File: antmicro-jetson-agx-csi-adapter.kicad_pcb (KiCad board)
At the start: 4 copper layers, 73.6 x 41 mm, 104 parts, among them IC1 MAX1708EEE+, J1 QTH-060-03-L-D-A, J2 WE_68715014522_ONE-SIDE, J3 WE_68715014022, J4 BM04B-SRSS-TB-LF-SN, J5 SM06B-SRSS-TB(LF)(SN), J6 SM09B-SRSS-TB(LF)(SN), J7 61300611121, Q1 BSS138AKA, U1 PCA9547BS,118, U2 NTS0102DP

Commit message: Routed all the signals
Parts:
- moved TP2 124.4 mm to (167.4, 107.6)
- moved TP3 121.9 mm to (167.4, 106.5)
- moved TP1 120.4 mm to (170.5, 105.6)
- moved TP7 119.9 mm to (170.5, 106.8)
- moved TP6 116.0 mm to (168.6, 103.9)
- moved TP4 110.2 mm to (167.4, 105.4)
- moved TP5 108.3 mm to (167.3, 103.9)
- moved TP9 104.8 mm to (160.4, 93.9)
- moved TP11 103.9 mm to (155.5, 72.2)
- moved TP10 99.5 mm to (149.0, 97.9)
- moved TP8 84.3 mm to (131.5, 104.2)
- moved TP23 81.0 mm to (154.2, 94.0)
- moved C6 17.1 mm to (150.1, 99.2), turned to 90 degrees
- moved TP21 11.8 mm to (152.8, 101.7), turned to 180 degrees
- moved U2 11.6 mm to (153.9, 99.1), turned to -90 degrees
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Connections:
- J1 pad G1: (no net) -> GND
- J1 pad G2: (no net) -> GND
- J1 pad G3: (no net) -> GND
- J1 pad G4: (no net) -> GND
- J1 pad G5: (no net) -> GND
- J1 pad G6: (no net) -> GND
- J1 pad G7: (no net) -> GND
- J1 pad G8: (no net) -> GND
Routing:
- net GND: track 7.58 -> 147.9 mm, vias 6 -> 79
- net /Auxiliary/DEPTH_CAM_SYNC_3V3: track 11.0 -> 67.6 mm, vias 0 -> 2
- net +3V3: track 3.10 -> 49.7 mm, vias 0 -> 21
- net DVDD_CAM_LV: track 0.00 -> 34.1 mm, vias 0 -> 1
- net AVDD_CAM_2V8: track 0.00 -> 24.9 mm, vias 0 -> 1
- net +1V8: track 6.16 -> 26.1 mm, vias 0 -> 1
- net /Interface/3V3_FFC_B: track 5.25 -> 17.1 mm, vias 0 -> 2
- net /Interface/I2C_GP2_CLK: track 0.00 -> 10.2 mm, vias 0 -> 1
- net I2C_GP3_CLK: track 17.4 -> 7.31 mm
- net /Interface/I2C_GP2_DAT: track 0.00 -> 9.44 mm, vias 0 -> 1
- net I2C_GP3_DAT: track 13.2 -> 4.17 mm
- net DVDD_CAM_IO: track 0.00 -> 8.92 mm, vias 0 -> 1
- net /Interface/CAM0_PWDN: track 0.00 -> 8.44 mm, vias 0 -> 1
- net CAM0_SDA: track 20.0 -> 28.4 mm
- net +5V: track 0.00 -> 6.97 mm, vias 0 -> 10
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- added copper zone on F.Cu, net +3V3
- added copper zone on In2.Cu, net +3V3
- added copper zone on B.Cu, net +5V
- added copper zone on F.Cu, net +5V
- added copper zone on In2.Cu, net +5V
- added copper zone on F.Cu, net /Interface/5V_FFC_B
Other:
- board text removed: "TODO: FIX FOOTPRINT"

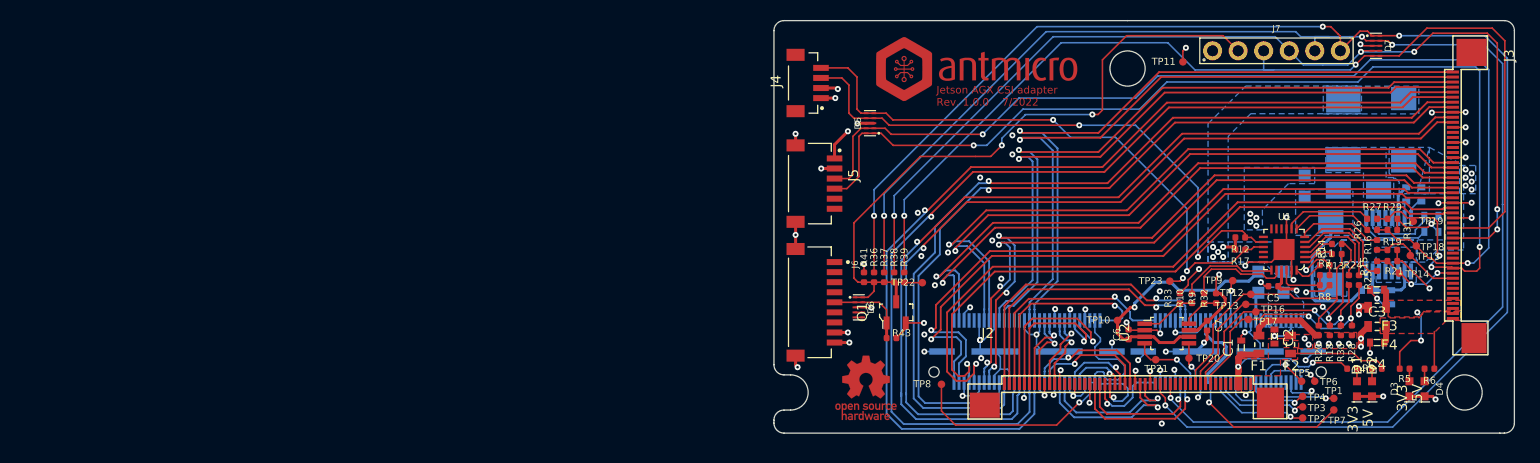
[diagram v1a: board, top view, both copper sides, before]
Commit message: Removed AUX connector and changed SYNC connector package
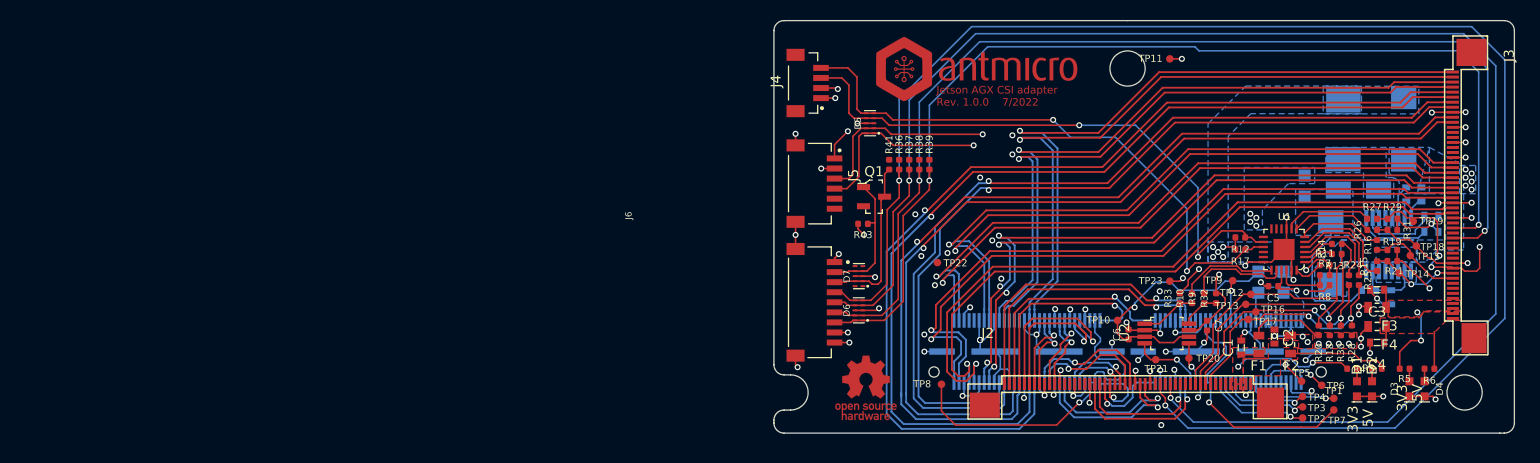
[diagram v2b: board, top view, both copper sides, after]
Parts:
- removed J7: 61300611121, antmicro-footprints:61300611121
- moved D7 56.3 mm to (123.3, 93.4), turned to 90 degrees
- moved Q1 11.7 mm to (124.8, 85.5), turned to 0 degrees
- moved R43 11.7 mm to (123.7, 88.2), turned to 0 degrees
- moved R37 11.5 mm to (128.3, 82.3), turned to 90 degrees
- moved R38 11.5 mm to (129.3, 82.3), turned to 90 degrees
- moved R39 11.5 mm to (130.3, 82.3), turned to 90 degrees
- moved R36 11.5 mm to (127.3, 82.3), turned to 90 degrees
- moved R41 11.5 mm to (126.3, 82.3)
- moved TP22 2.50 mm to (131.1, 92.1)
- moved TP11 1.33 mm to (154.2, 71.9)
- moved TP6 0.81 mm to (169.3, 104.3)
- moved D6 0.30 mm to (123.3, 96.8), turned to 90 degrees
- moved C8 0.10 mm to (177.4, 78.8)
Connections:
- D6 pad 1: /Auxiliary/DEPTH_CAM_SYNC_3V3 -> VSYNC_CAM3_3V3
- D6 pad 10: /Auxiliary/DEPTH_CAM_SYNC_3V3 -> VSYNC_CAM3_3V3
- D6 pad 2: /Auxiliary/DEPTH_CAM_SYNC -> VSYNC_CAM2_3V3
- D6 pad 4: Net-(D6-Pad4) -> VSYNC_CAM1_3V3
- D6 pad 5: Net-(D6-Pad5) -> VSYNC_CAM0_3V3
- D6 pad 6: Net-(D6-Pad5) -> VSYNC_CAM0_3V3
- D6 pad 7: Net-(D6-Pad4) -> VSYNC_CAM1_3V3
- D6 pad 9: /Auxiliary/DEPTH_CAM_SYNC -> VSYNC_CAM2_3V3
- D7 pad 1: VSYNC_CAM0_3V3 -> unconnected-(D7-Pad1)
- D7 pad 10: VSYNC_CAM0_3V3 -> unconnected-(D7-Pad1)
- D7 pad 2: VSYNC_CAM1_3V3 -> /Auxiliary/CAM_SYNC_3V3
- D7 pad 4: VSYNC_CAM2_3V3 -> /Auxiliary/CAM_SYNC
- D7 pad 5: VSYNC_CAM3_3V3 -> unconnected-(D7-Pad5)
- D7 pad 6: VSYNC_CAM3_3V3 -> unconnected-(D7-Pad5)
- D7 pad 7: VSYNC_CAM2_3V3 -> /Auxiliary/CAM_SYNC
- D7 pad 9: VSYNC_CAM1_3V3 -> /Auxiliary/CAM_SYNC_3V3
- J1 pad G1: GND -> (no net)
- J1 pad G2: GND -> (no net)
- J1 pad G3: GND -> (no net)
- J1 pad G4: GND -> (no net)
- J1 pad G5: GND -> (no net)
- J1 pad G6: GND -> (no net)
- J1 pad G7: GND -> (no net)
- J1 pad G8: GND -> (no net)
- J6 pad 1: /Auxiliary/GPIO3 -> GND
- J6 pad 2: /Auxiliary/GPIO4 -> /Auxiliary/CAM_SYNC
- J6 pad 3: /Auxiliary/GPIO5 -> /Auxiliary/CAM_SYNC_3V3
- J6 pad 4: /Auxiliary/GPIO6 -> VSYNC_CAM0_3V3
- J6 pad 5: /Auxiliary/DEPTH_CAM_SYNC -> VSYNC_CAM1_3V3
- J6 pad 6: /Auxiliary/LASER_PWM0 -> VSYNC_CAM2_3V3
- J6 pad 7: /Auxiliary/LASER_PWM1 -> VSYNC_CAM3_3V3
- Q1 pad 1: /Auxiliary/DEPTH_CAM_SYNC -> /Auxiliary/CAM_SYNC
- Q1 pad 3: /Auxiliary/DEPTH_CAM_SYNC_3V3 -> /Auxiliary/CAM_SYNC_3V3
- R36 pad 2: /Auxiliary/DEPTH_CAM_SYNC_3V3 -> /Auxiliary/CAM_SYNC_3V3
- R37 pad 2: /Auxiliary/DEPTH_CAM_SYNC_3V3 -> /Auxiliary/CAM_SYNC_3V3
- R38 pad 2: /Auxiliary/DEPTH_CAM_SYNC_3V3 -> /Auxiliary/CAM_SYNC_3V3
- R39 pad 2: /Auxiliary/DEPTH_CAM_SYNC_3V3 -> /Auxiliary/CAM_SYNC_3V3
- R41 pad 1: /Auxiliary/DEPTH_CAM_SYNC_3V3 -> /Auxiliary/CAM_SYNC_3V3
- R43 pad 2: /Auxiliary/DEPTH_CAM_SYNC -> /Auxiliary/CAM_SYNC
- TP22 pad 1: /Auxiliary/DEPTH_CAM_SYNC_3V3 -> /Auxiliary/CAM_SYNC_3V3
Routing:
- net CAM3_SDA: track 103.9 -> 29.7 mm
- net CAM3_SCL: track 108.9 -> 37.8 mm
- net /Auxiliary/DEPTH_CAM_SYNC_3V3: track 67.6 -> 0.00 mm, vias 2 -> 0
- net /Auxiliary/CAM_SYNC_3V3: track 0.00 -> 16.5 mm
- net /Auxiliary/CAM_SYNC: track 0.00 -> 13.3 mm
- net VSYNC_CAM0_3V3: track 148.9 -> 158.0 mm, vias 4 -> 2
- net VSYNC_CAM1_3V3: track 144.5 -> 153.2 mm, vias 4 -> 2
- net /Auxiliary/DEPTH_CAM_SYNC: track 8.29 -> 0.00 mm
- net VSYNC_CAM2_3V3: track 102.2 -> 108.5 mm, vias 5 -> 2
- net VSYNC_CAM3_3V3: track 102.4 -> 105.1 mm
- net /Interface/3V3_FFC_B: track 17.1 -> 14.6 mm
- net GND: track 147.9 -> 146.7 mm
- net +3V3: track 49.7 -> 48.6 mm, vias 21 -> 20
- net Net-(D6-Pad5): track 0.77 -> 0.00 mm
- net Net-(D6-Pad4): track 0.77 -> 0.00 mm
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- added copper zone on F.Cu, net /Interface/3V3_FFC_B

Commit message: Rerouted tracks after connector change
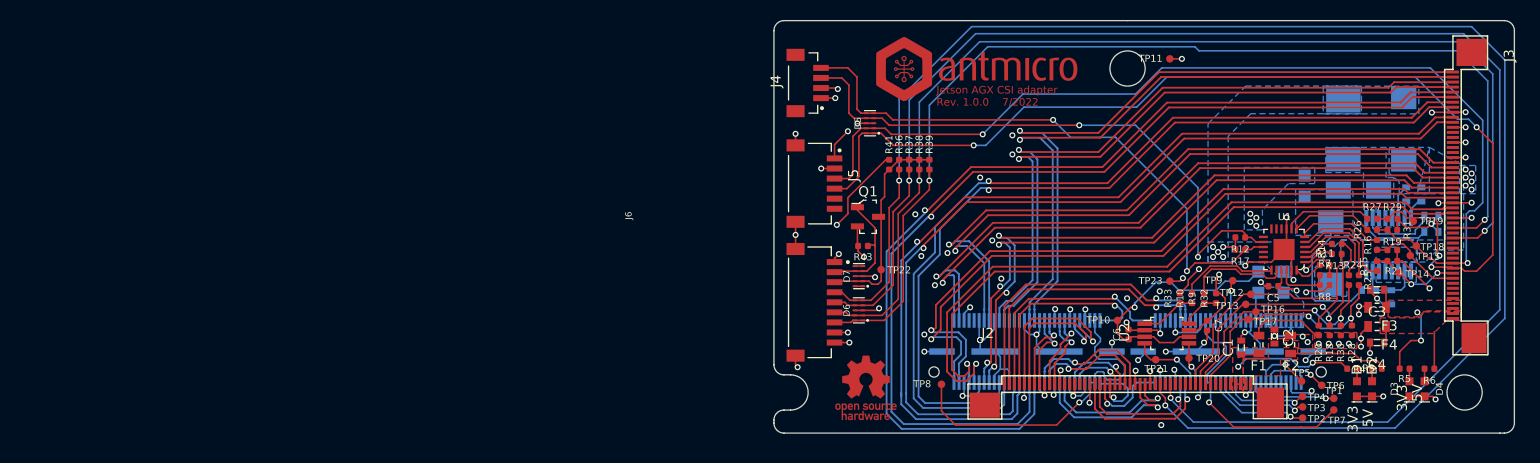
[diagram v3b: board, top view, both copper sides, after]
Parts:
- moved TP22 5.64 mm to (125.5, 92.8)
- moved R43 2.20 mm to (123.7, 90.4)
- moved Q1 2.09 mm to (124.2, 87.5)
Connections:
- J1 pad G1: (no net) -> GND
- J1 pad G2: (no net) -> GND
- J1 pad G3: (no net) -> GND
- J1 pad G4: (no net) -> GND
- J1 pad G5: (no net) -> GND
- J1 pad G6: (no net) -> GND
- J1 pad G7: (no net) -> GND
- J1 pad G8: (no net) -> GND
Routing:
- net CAM3_SDA: track 29.7 -> 99.5 mm
- net CAM3_SCL: track 37.8 -> 105.7 mm
- net +3V3: track 48.6 -> 57.4 mm, vias 20 -> 21
- net /Auxiliary/CAM_SYNC_3V3: track 16.5 -> 20.7 mm
- net GND: track 146.7 -> 148.7 mm
- net /Auxiliary/CAM_SYNC: track 13.3 -> 11.5 mm
- net VSYNC_CAM3_3V3: track 105.1 -> 105.9 mm
- net unconnected-(D7-Pad5): track 0.00 -> 0.78 mm
- net unconnected-(D7-Pad1): track 0.00 -> 0.78 mm

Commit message: Length matched CSI signals
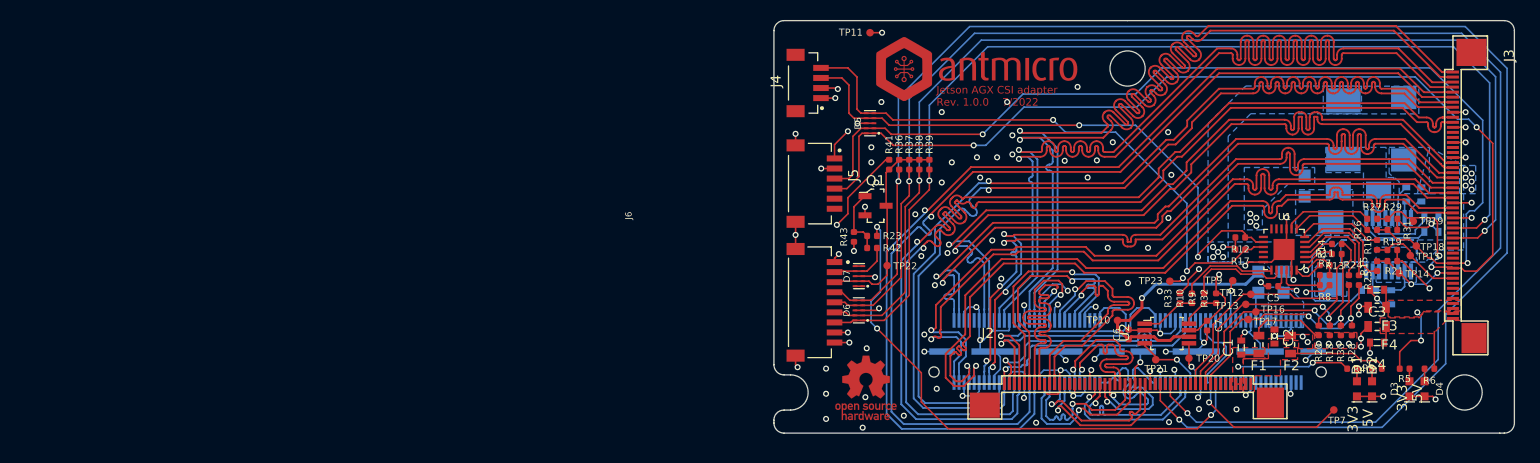
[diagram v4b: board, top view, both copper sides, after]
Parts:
- removed TP1, TP2, TP3, TP4, TP5, TP6, TP8: TP_SMD_0_75MM, antmicro-footprints:Testpoint_smd_0_75mm
- added R23: R_0R_0402, antmicro-footprints:0402-res, F.Cu at (124.6, 89.4)
- added R42: R_0R_0402, antmicro-footprints:0402-res, F.Cu at (124.6, 90.6)
- moved TP11 29.9 mm to (124.4, 69.3)
- moved Q1 1.33 mm to (125.0, 86.4)
- moved R43 1.27 mm to (122.8, 89.5), turned to 90 degrees
- moved TP22 0.72 mm to (126.1, 92.4)
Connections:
- D7 pad 4: /Auxiliary/CAM_SYNC -> /Auxiliary/EXT_CAM_SYNC
- D7 pad 7: /Auxiliary/CAM_SYNC -> /Auxiliary/EXT_CAM_SYNC
- J1 pad 101: DVDD_CAM_IO -> unconnected-(J1-Pad101)
- J1 pad 103: /Interface/SNN_FLASH_MASK -> unconnected-(J1-Pad103)
- J1 pad 104: /Interface/SNN_TORCH_EN -> unconnected-(J1-Pad104)
- J1 pad 105: /Interface/I2C_GP4_CLK -> unconnected-(J1-Pad105)
- J1 pad 106: /Interface/SNN_FLASH_STROBE -> unconnected-(J1-Pad106)
- J1 pad 107: /Interface/I2C_GP4_DAT -> unconnected-(J1-Pad107)
- J1 pad 109: /Interface/VDD_IR -> unconnected-(J1-Pad109)
- J1 pad 111: /Interface/SNN_SPI_SCK -> unconnected-(J1-Pad111)
- J1 pad 112: /Interface/SNN_SPI_DIN -> unconnected-(J1-Pad112)
- J1 pad 113: /Interface/SNN_SPI_CS0 -> unconnected-(J1-Pad113)
- J1 pad 114: /Interface/SNN_SPI_DOUT -> unconnected-(J1-Pad114)
- J1 pad 117: /Interface/CAM_INTR -> unconnected-(J1-Pad117)
- J1 pad 119: /Interface/GPIO25_VDD_SYS_EN -> unconnected-(J1-Pad119)
- J1 pad 55: DVDD_CAM_LV -> unconnected-(J1-Pad55)
- J1 pad 56: DVDD_CAM_LV -> unconnected-(J1-Pad56)
- J1 pad 57: DVDD_CAM_LV -> unconnected-(J1-Pad57)
- J1 pad 58: DVDD_CAM_LV -> unconnected-(J1-Pad58)
- J1 pad 76: /Interface/SNN_CAM_76 -> unconnected-(J1-Pad76)
- J1 pad 78: /Interface/SNN_CAM_HSYNC -> unconnected-(J1-Pad78)
- J1 pad 84: /Interface/VDD_AF -> unconnected-(J1-Pad84)
- J1 pad 85: /Interface/CAM_AF_PWDN -> GPIO10
- J1 pad 86: /Interface/SNN_CAM_VSYNC -> unconnected-(J1-Pad86)
- J1 pad 87: /Interface/I2C_GP2_CLK -> unconnected-(J1-Pad87)
- J1 pad 88: /Interface/CAM1_MCLK03 -> unconnected-(J1-Pad88)
- J1 pad 89: /Interface/I2C_GP2_DAT -> unconnected-(J1-Pad89)
- J1 pad 90: /Interface/CAM1_PWDN -> unconnected-(J1-Pad90)
- J1 pad 91: /Interface/CAM0_MCLK02 -> unconnected-(J1-Pad91)
- J1 pad 93: /Interface/CAM0_PWDN -> unconnected-(J1-Pad93)
- J1 pad 94: /Interface/CAM2_MCLK04 -> unconnected-(J1-Pad94)
- J1 pad 95: /Interface/CAM0_RST_BUFFER -> unconnected-(J1-Pad95)
- J1 pad 96: /Interface/SNN_CAM2_PWDN -> unconnected-(J1-Pad96)
- J1 pad 97: /Interface/SNN_FLASH_EN -> unconnected-(J1-Pad97)
- J1 pad 98: /Interface/SNN_CAM2_RST -> unconnected-(J1-Pad98)
- J6 pad 2: /Auxiliary/CAM_SYNC -> /Auxiliary/EXT_CAM_SYNC
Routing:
- net GPIO10: track 0.00 -> 54.8 mm, vias 0 -> 3
- net /Interface/CSI3_D0_P: track 65.2 -> 99.7 mm
- net DVDD_CAM_LV: track 34.1 -> 0.00 mm, vias 1 -> 0
- net /Interface/CSI3_D0_N: track 66.0 -> 99.7 mm
- net /Interface/CSI3_D1_P: track 67.4 -> 99.9 mm
- net /Interface/CSI3_D1_N: track 68.2 -> 99.9 mm
- net /Interface/CSI6_CLK_P: track 7.92 -> 23.9 mm
- net /Interface/CSI6_D0_N: track 7.84 -> 23.8 mm
- net /Interface/CSI6_CLK_N: track 8.04 -> 23.9 mm
- net /Interface/CSI2_D0_P: track 84.6 -> 100.4 mm
- net /Interface/CSI6_D0_P: track 7.98 -> 23.8 mm
- net /Interface/CSI2_D0_N: track 87.0 -> 100.5 mm
- net /Interface/CSI1_D0_P: track 62.1 -> 73.8 mm
- net /Interface/CSI2_CLK_P: track 88.5 -> 100.2 mm
- net /Interface/CSI4_D1_N: track 5.77 -> 16.0 mm
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
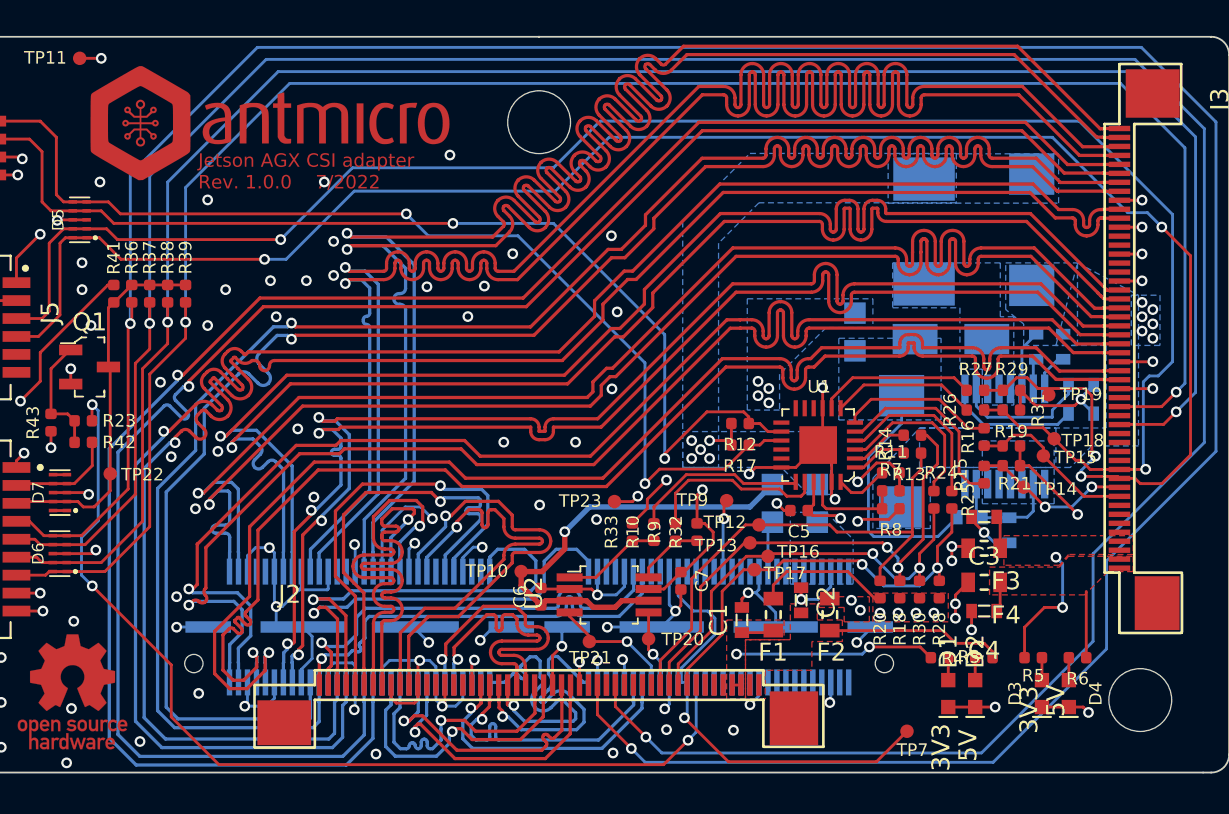
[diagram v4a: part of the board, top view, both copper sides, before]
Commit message: Filleted CSI tracks
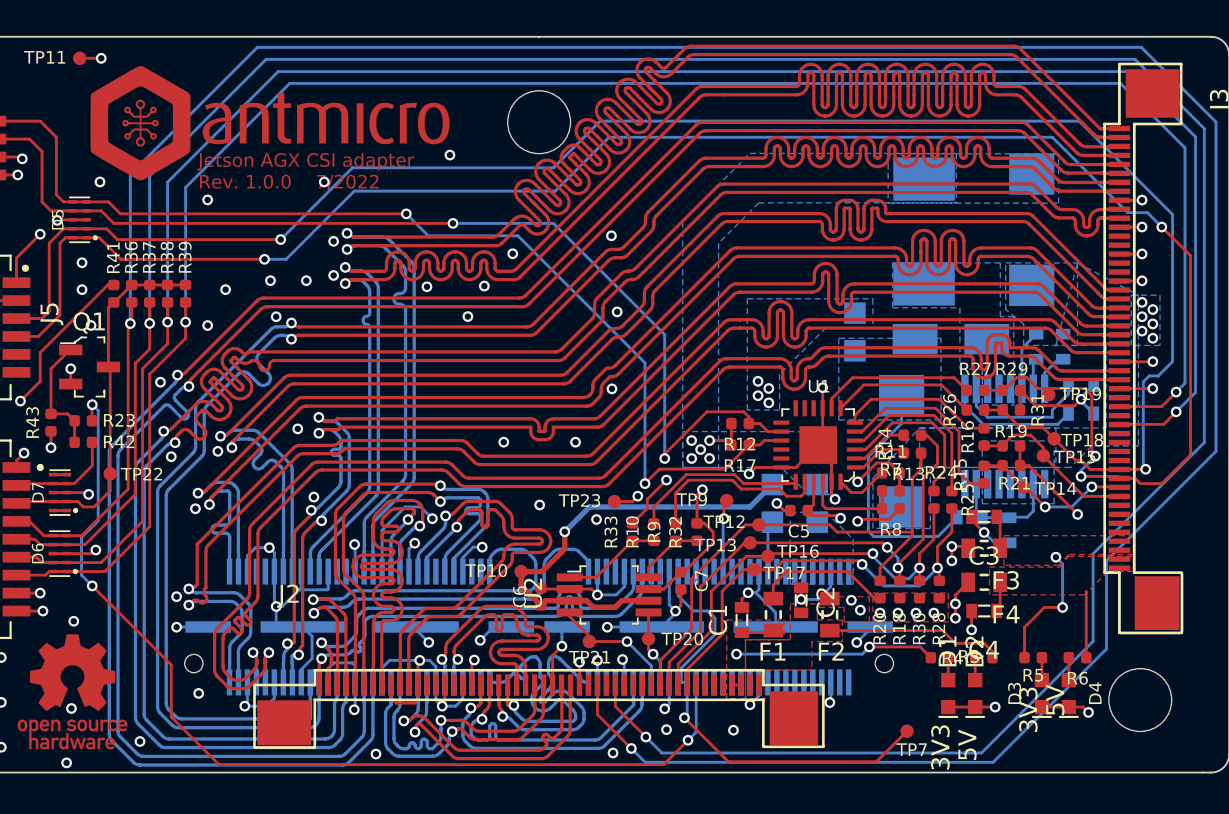
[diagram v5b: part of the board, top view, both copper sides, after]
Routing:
- net /Interface/CSI3_D0_P: track 99.7 -> 99.1 mm
- net /Interface/CSI3_D0_N: track 99.7 -> 99.1 mm
